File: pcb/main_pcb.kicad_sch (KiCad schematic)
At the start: 29 parts, among them J1 Conn_01x06_Socket, J2 Conn_01x10_Pin, J3 Conn_01x06_Pin, J4 USB_C_Receptacle_USB2.0, SW1 SW_Push, SW2 SW_Push, SW3 SW_Push, U1 ESP32-H2-MINI-1, U2 LM5165Y

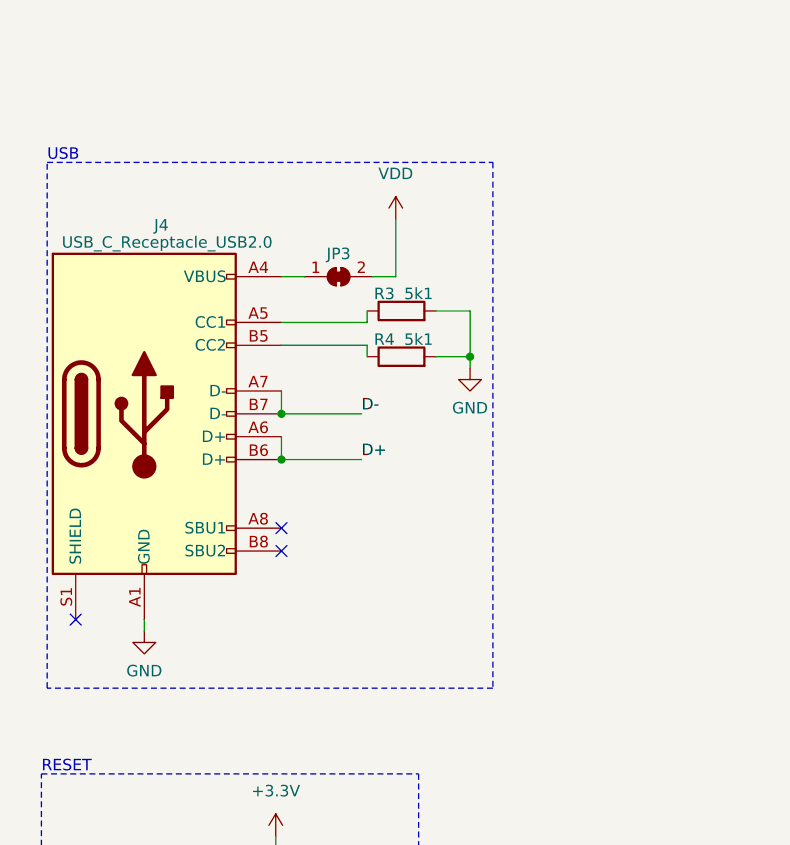
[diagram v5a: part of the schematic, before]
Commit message: Add ESD protection to USB data lines
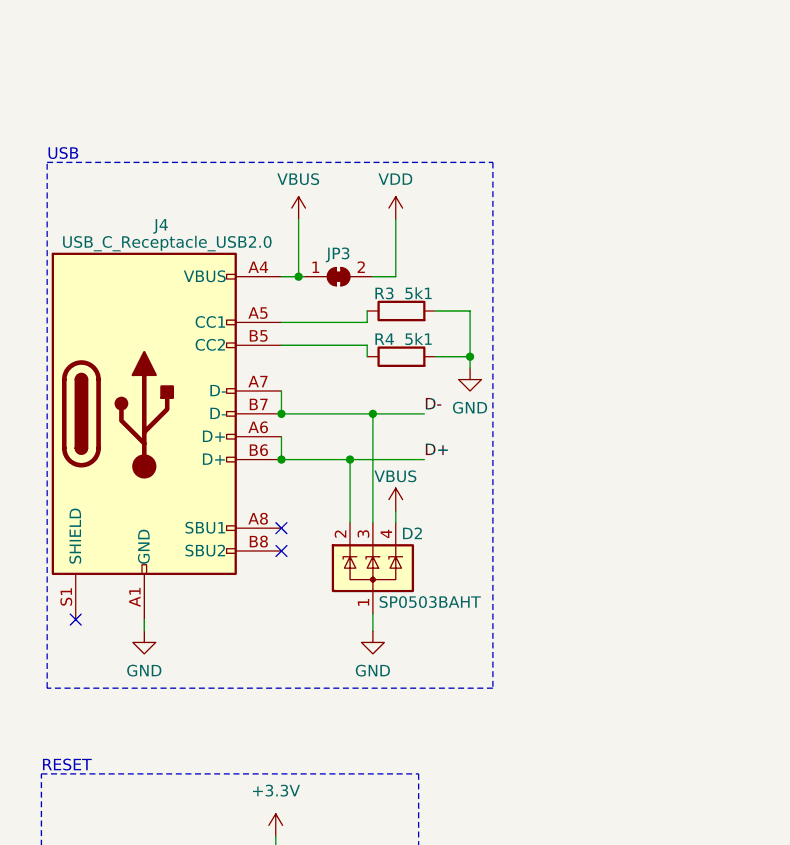
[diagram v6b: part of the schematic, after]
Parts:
- added D2: SP0503BAHT, Package_TO_SOT_SMD:SOT-143, symbol Power_Protection:SP0503BAHT
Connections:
- net D+: now also D2.2 (K)
- net D-: now also D2.3 (K)
- net GND: now also D2.1 (A)
- net VBUS: now reaches J4.A4 (VBUS), J4.A9 (VBUS), J4.B4 (VBUS), J4.B9 (VBUS), JP3.1 (A)
- net VBUS: now also D2.4 (K)
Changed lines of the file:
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@@
   (junction (at 167.64 40.64) (diameter 0) (color 0 0 0 0)
   )
+  (junction (at 58.42 79.375) (diameter 0) (color 0 0 0 0)
+  )
   (junction (at 47.625 140.335) (diameter 0) (color 0 0 0 0)
   )
@@
   (junction (at 34.925 140.335) (diameter 0) (color 0 0 0 0)
   )
+  (junction (at 50.165 64.135) (diameter 0) (color 0 0 0 0)
+  )
   (junction (at 198.755 175.26) (diameter 0) (color 0 0 0 0)
   )
@@
   )
   (junction (at 29.845 153.035) (diameter 0) (color 0 0 0 0)
+  )
+  (junction (at 55.88 84.455) (diameter 0) (color 0 0 0 0)
   )
   (junction (at 37.465 257.175) (diameter 0) (color 0 0 0 0)
@@
     (stroke (width 0) (type default))
   )
+  (wire (pts (xy 58.42 79.375) (xy 58.42 91.44))
+    (stroke (width 0) (type default))
+  )
   (wire (pts (xy 193.04 69.85) (xy 207.01 69.85))
     (stroke (width 0) (type default))
@@
     (stroke (width 0) (type default))
   )
+  (wire (pts (xy 60.96 90.17) (xy 60.96 91.44))
+    (stroke (width 0) (type default))
+  )
   (wire (pts (xy 47.625 140.335) (xy 56.515 140.335))
     (stroke (width 0) (type default))
@@
     (stroke (width 0) (type default))
   )
-  (wire (pts (xy 48.26 64.135) (xy 50.8 64.135))
+  (wire (pts (xy 48.26 64.135) (xy 50.165 64.135))
     (stroke (width 0) (type default))
   )
@@
     (stroke (width 0) (type default))
   )
+  (wire (pts (xy 58.42 79.375) (xy 64.135 79.375))
+    (stroke (width 0) (type default))
+  )
   (wire (pts (xy 32.385 198.755) (xy 45.085 198.755))
     (stroke (width 0) (type default))
@@
     (stroke (width 0) (type default))
   )
+  (wire (pts (xy 50.165 64.135) (xy 50.8 64.135))
+    (stroke (width 0) (type default))
+  )
   (wire (pts (xy 29.845 247.015) (xy 37.465 247.015))
     (stroke (width 0) (type default))
@@
     (stroke (width 0) (type default))
   )
+  (wire (pts (xy 55.88 84.455) (xy 55.88 91.44))
+    (stroke (width 0) (type default))
+  )
   (wire (pts (xy 167.005 177.8) (xy 165.735 177.8))
     (stroke (width 0) (type default))
@@
     (stroke (width 0) (type default))
   )
+  (wire (pts (xy 50.165 57.785) (xy 50.165 64.135))
+    (stroke (width 0) (type default))
+  )
   (wire (pts (xy 81.915 217.805) (xy 89.535 217.805))
     (stroke (width 0) (type default))
   )
-  (wire (pts (xy 48.26 79.375) (xy 57.15 79.375))
+  (wire (pts (xy 48.26 79.375) (xy 58.42 79.375))
     (stroke (width 0) (type default))
   )
@@
     (stroke (width 0) (type default))
   )
+  (wire (pts (xy 58.42 101.6) (xy 58.42 103.505))
+    (stroke (width 0) (type default))
+  )
   (wire (pts (xy 29.845 244.475) (xy 46.355 244.475))
     (stroke (width 0) (type default))
@@
     (stroke (width 0) (type default))
   )
+  (wire (pts (xy 55.88 84.455) (xy 64.135 84.455))
+    (stroke (width 0) (type default))
+  )
   (wire (pts (xy 86.995 222.885) (xy 86.995 220.345))
     (stroke (width 0) (type default))
@@
     (stroke (width 0) (type default))
   )
-  (wire (pts (xy 48.26 84.455) (xy 57.15 84.455))
+  (wire (pts (xy 48.26 84.455) (xy 55.88 84.455))
     (stroke (width 0) (type default))
   )
@@
     (effects (font (size 1.27 1.27)) (justify left bottom))
   )
-  (label "D+" (at 57.15 84.455 0) (fields_autoplaced)
+  (label "D+" (at 64.135 84.455 0) (fields_autoplaced)
     (effects (font (size 1.27 1.27)) (justify left bottom))
   )
@@
     (effects (font (size 1.27 1.27)) (justify left bottom))
   )
-  (label "D-" (at 57.15 79.375 0) (fields_autoplaced)
+  (label "D-" (at 64.135 79.375 0) (fields_autoplaced)
     (effects (font (size 1.27 1.27)) (justify left bottom))
   )
@@
   )
   (symbol (lib_id "power:VDD") (at 60.96 57.785 0) (unit 1)
-    (in_bom yes) (on_board yes) (dnp no) (fields_autoplaced)
+    (in_bom yes) (on_board yes) (dnp no)
     (property "Reference" "#PWR023" (at 60.96 61.595 0)
       (effects (font (size 1.27 1.27)) hide)
     )
-    (property "Value" "VDD" (at 60.96 52.705 0)
+    (property "Value" "VDD" (at 60.96 53.34 0)
       (effects (font (size 1.27 1.27)))
     )
@@
         (path "/6204b7c2-8814-41ee-9243-5078f55f08d4"
           (reference "R6") (unit 1)
+        )
+      )
+    )
+  )
+  (symbol (lib_id "power:VBUS") (at 50.165 57.785 0) (unit 1)
+    (in_bom yes) (on_board yes) (dnp no) (fields_autoplaced)
+    (property "Reference" "#PWR029" (at 50.165 61.595 0)
+      (effects (font (size 1.27 1.27)) hide)
+    )
+    (property "Value" "VBUS" (at 50.165 53.34 0)
+      (effects (font (size 1.27 1.27)))
+    )
+    (property "Footprint" "" (at 50.165 57.785 0)
+      (effects (font (size 1.27 1.27)) hide)
+    )
+    (property "Datasheet" "" (at 50.165 57.785 0)
+      (effects (font (size 1.27 1.27)) hide)
+    )
+    (pin "1")
+    (instances
+      (project "main_pcb"
+        (path "/6204b7c2-8814-41ee-9243-5078f55f08d4"
+          (reference "#PWR029") (unit 1)
         )
       )
@@
     )
   )
+  (symbol (lib_id "power:GND") (at 58.42 103.505 0) (unit 1)
+    (in_bom yes) (on_board yes) (dnp no) (fields_autoplaced)
+    (property "Reference" "#PWR027" (at 58.42 109.855 0)
+      (effects (font (size 1.27 1.27)) hide)
+    )
+    (property "Value" "GND" (at 58.42 107.95 0)
+      (effects (font (size 1.27 1.27)))
+    )
+    (property "Footprint" "" (at 58.42 103.505 0)
+      (effects (font (size 1.27 1.27)) hide)
+    )
+    (property "Datasheet" "" (at 58.42 103.505 0)
+      (effects (font (size 1.27 1.27)) hide)
+    )
+    (pin "1")
+    (instances
+      (project "main_pcb"
+        (path "/6204b7c2-8814-41ee-9243-5078f55f08d4"
+          (reference "#PWR027") (unit 1)
+        )
+      )
+    )
+  )
+  (symbol (lib_id "power:VBUS") (at 60.96 90.17 0) (unit 1)
+    (in_bom yes) (on_board yes) (dnp no)
+    (property "Reference" "#PWR028" (at 60.96 93.98 0)
+      (effects (font (size 1.27 1.27)) hide)
+    )
+    (property "Value" "VBUS" (at 60.96 86.36 0)
+      (effects (font (size 1.27 1.27)))
+    )
+    (property "Footprint" "" (at 60.96 90.17 0)
+      (effects (font (size 1.27 1.27)) hide)
+    )
+    (property "Datasheet" "" (at 60.96 90.17 0)
+      (effects (font (size 1.27 1.27)) hide)
+    )
+    (pin "1")
+    (instances
+      (project "main_pcb"
+        (path "/6204b7c2-8814-41ee-9243-5078f55f08d4"
+          (reference "#PWR028") (unit 1)
+        )
+      )
+    )
+  )
   (symbol (lib_id "power:GND") (at 229.235 199.39 0) (unit 1)
     (in_bom yes) (on_board yes) (dnp no) (fields_autoplaced)
@@
         )
       )
+    )
+  )
+  (symbol (lib_id "Power_Protection:SP0503BAHT") (at 58.42 96.52 0) (unit 1)
+    (in_bom yes) (on_board yes) (dnp no)
+    (property "Reference" "D2" (at 61.595 92.71 0)
+      (effects (font (size 1.27 1.27)) (justify left))
+    )
+    (property "Value" "SP0503BAHT" (at 59.055 100.33 0)
+      (effects (font (size 1.27 1.27)) (justify left))
+    )
+    (property "Footprint" "Package_TO_SOT_SMD:SOT-143" (at 64.135 97.79 0)
+      (effects (font (size 1.27 1.27)) (justify left) hide)
+    )
+    (property "Datasheet" "http://www.littelfuse.com/~/media/files/littelfuse/technical%20resources/documents/data%20sheets/sp05xxba.pdf" (at 61.595 93.345 0)
+      (effects (font (size 1.27 1.27)) hide)
+    )
+    (pin "3")
+    (pin "1")
+    (pin "2")
+    (pin "4")
+    (instances
+      (project "main_pcb"
+        (path "/6204b7c2-8814-41ee-9243-5078f55f08d4"
+          (reference "D2") (unit 1)
+        )
+      )

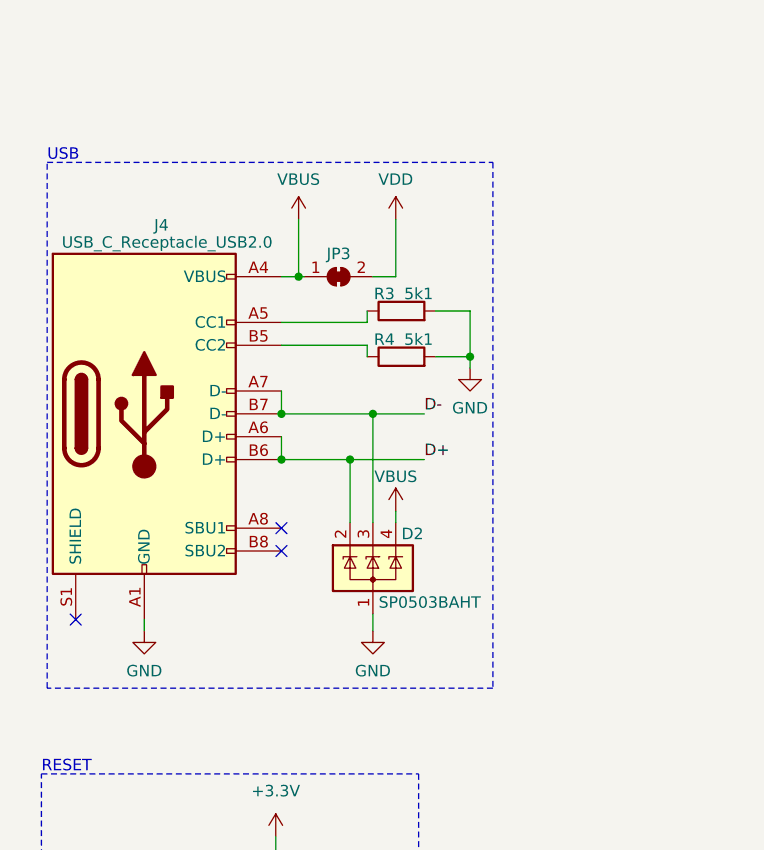
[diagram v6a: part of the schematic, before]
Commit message: Improve USB circuit
Add reverse voltage protection and VBUS capacitor.
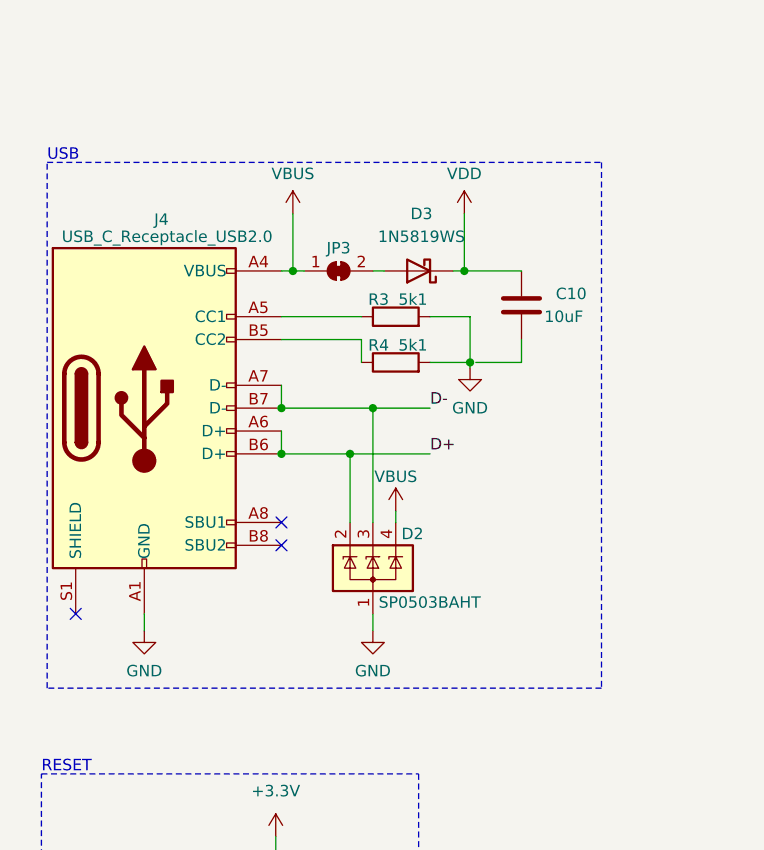
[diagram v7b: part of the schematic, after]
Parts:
- added C10: 10uF, Capacitor_SMD:C_1206_3216Metric_Pad1.33x1.80mm_HandSolder, symbol Device:C
- added D3: 1N5819WS, Diode_SMD:D_SOD-323, symbol Diode:1N5819WS
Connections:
- net VDD: now also C10.1, D3.1 (K); no longer JP3.2 (B)
- new net: D3.2 (A), JP3.2 (B)
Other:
- moved on the sheet: J4, JP3, R3, R4

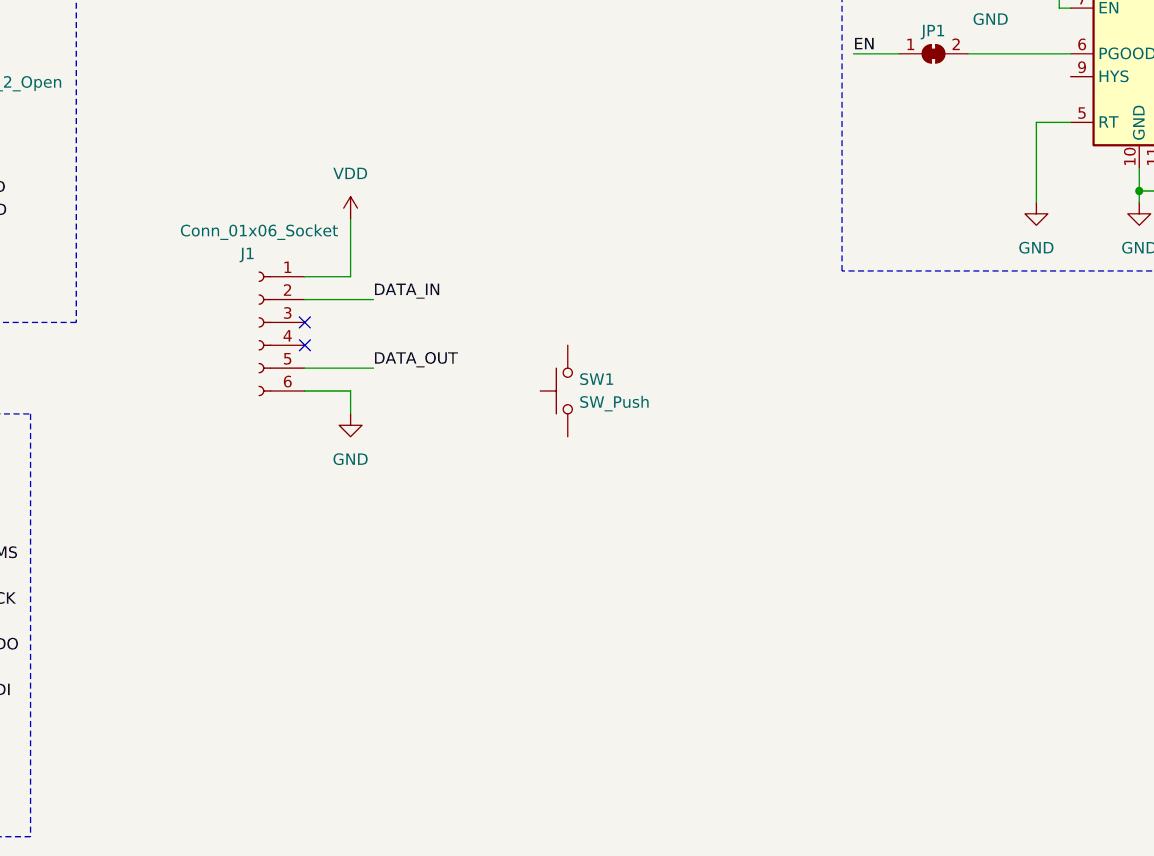
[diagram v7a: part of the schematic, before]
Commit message: Add reverse current protection to HAN-interface
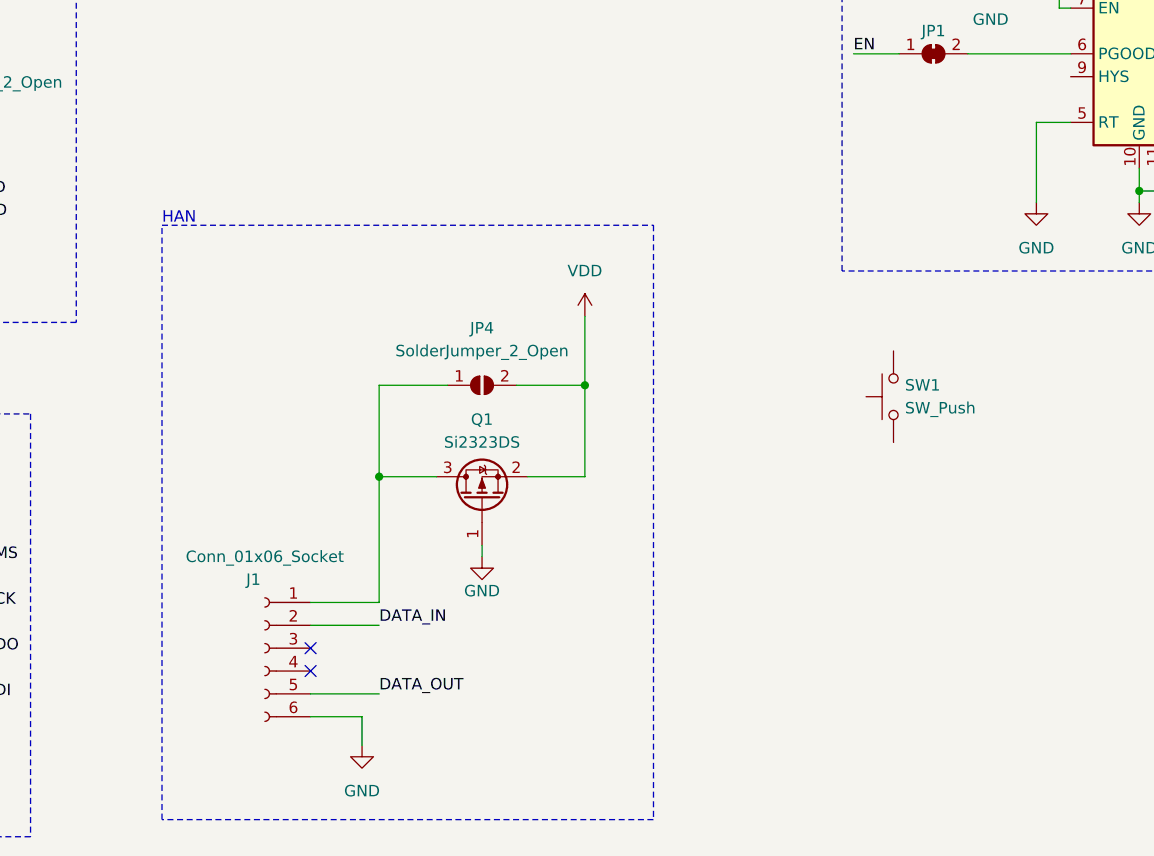
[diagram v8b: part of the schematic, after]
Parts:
- added JP4: SolderJumper_2_Open, Jumper:SolderJumper-2_P1.3mm_Open_TrianglePad1.0x1.5mm, symbol Jumper:SolderJumper_2_Open
- added Q1: Si2323DS, Package_TO_SOT_SMD:SOT-23, symbol zk:Si2323DS
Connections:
- net GND: now also Q1.1 (G)
- net VDD: now also JP4.2 (B), Q1.2 (S); no longer J1.1 (Pin_1)
- new net: J1.1 (Pin_1), JP4.1 (A), Q1.3 (D)
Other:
- note added: "HAN"
- moved on the sheet: J1, SW1
